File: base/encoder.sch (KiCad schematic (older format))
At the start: 4 parts

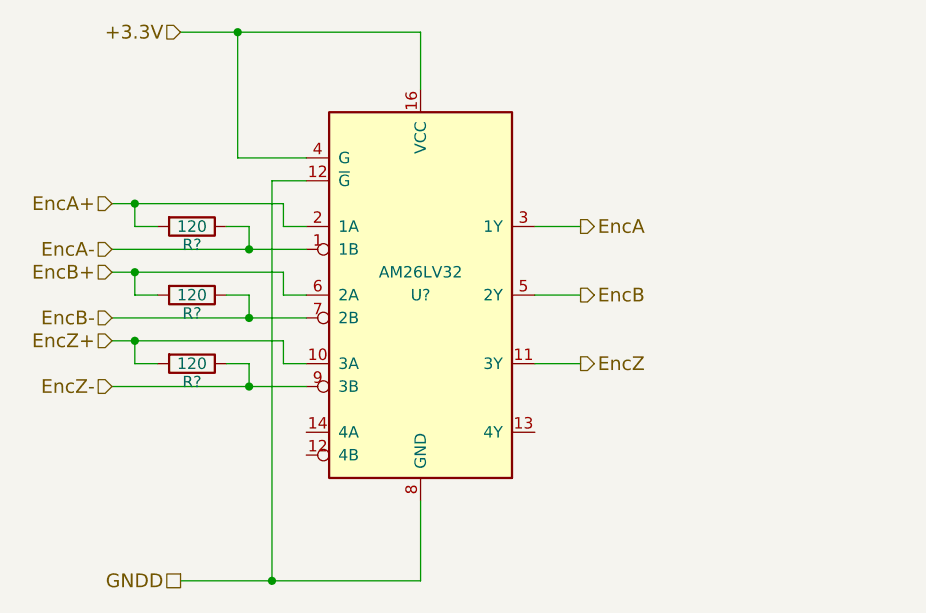
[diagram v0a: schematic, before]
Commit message: Update base board: 1. Add extra analog voltage input to core board.   -> update pinmux 2. Assign most footprints. 3. Generate netlist. 4. Add core_sf board. 5. Add kicad_symbols library submodule.
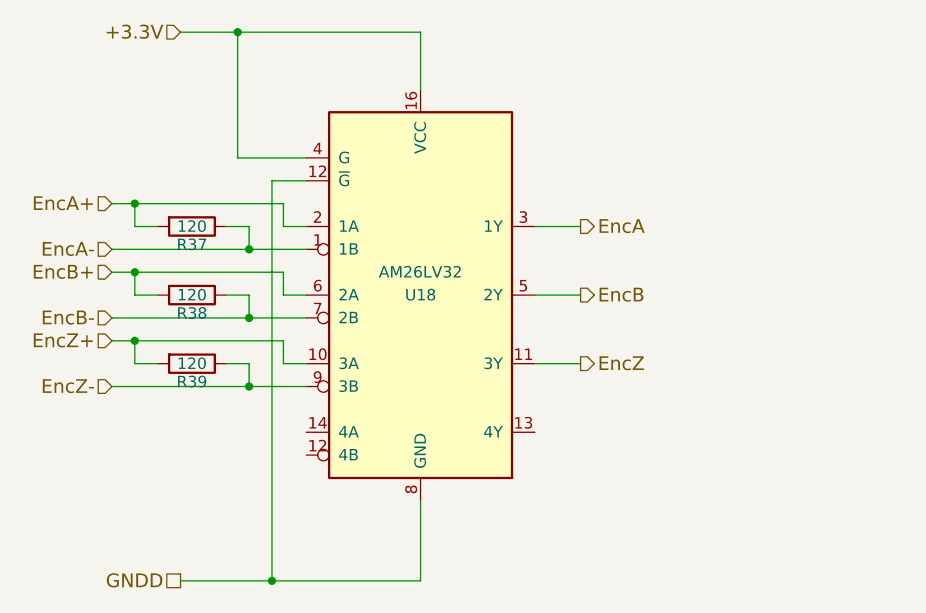
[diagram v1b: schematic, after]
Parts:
- R37, R38, R39: renamed from R?; footprint (none) -> Resistor_SMD:R_0603_1608Metric
- U18: renamed from U?; footprint Housings_SOIC:SOIC-16_3.9x9.9mm_Pitch1.27mm -> Package_SOIC:SOIC-16_3.9x9.9mm_P1.27mm
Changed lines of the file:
@@
 GNDD
 $Comp
-L AM26LV32 U?
+L AM26LV32 U18
 U 1 1 5A42515F
 P 4800 3250
-F 0 "U?" H 4800 3250 50  0000 C CNN
+F 0 "U18" H 4800 3250 50  0000 C CNN
 F 1 "AM26LV32" H 4800 3350 50  0000 C CNN
-F 2 "Housings_SOIC:SOIC-16_3.9x9.9mm_Pitch1.27mm" H 4900 2300 50  0001 C CNN
+F 2 "Package_SOIC:SOIC-16_3.9x9.9mm_P1.27mm" H 4900 2300 50  0001 C CNN
 F 3 "" H 4800 3250 50  0001 C CNN
 	1    4800 3250
@@
 Connection ~ 4150 4500
 $Comp
-L R R?
+L R R37
 U 1 1 5A425215
 P 3800 2950
-F 0 "R?" V 3880 2950 50  0000 C CNN
+F 0 "R37" V 3880 2950 50  0000 C CNN
 F 1 "120" V 3800 2950 50  0000 C CNN
-F 2 "" V 3730 2950 50  0001 C CNN
+F 2 "Resistor_SMD:R_0603_1608Metric" V 3730 2950 50  0001 C CNN
 F 3 "" H 3800 2950 50  0001 C CNN
 	1    3800 2950
@@
 	3450 3350 4300 3350
 $Comp
-L R R?
+L R R38
 U 1 1 5A425315
 P 3800 3250
-F 0 "R?" V 3880 3250 50  0000 C CNN
+F 0 "R38" V 3880 3250 50  0000 C CNN
 F 1 "120" V 3800 3250 50  0000 C CNN
-F 2 "" V 3730 3250 50  0001 C CNN
+F 2 "Resistor_SMD:R_0603_1608Metric" V 3730 3250 50  0001 C CNN
 F 3 "" H 3800 3250 50  0001 C CNN
 	1    3800 3250
@@
 	4300 3650 3450 3650
 $Comp
-L R R?
+L R R39
 U 1 1 5A425470
 P 3800 3550
-F 0 "R?" V 3880 3550 50  0000 C CNN
+F 0 "R39" V 3880 3550 50  0000 C CNN
 F 1 "120" V 3800 3550 50  0000 C CNN
-F 2 "" V 3730 3550 50  0001 C CNN
+F 2 "Resistor_SMD:R_0603_1608Metric" V 3730 3550 50  0001 C CNN
 F 3 "" H 3800 3550 50  0001 C CNN
 	1    3800 3550

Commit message: temp-sens-fan was created
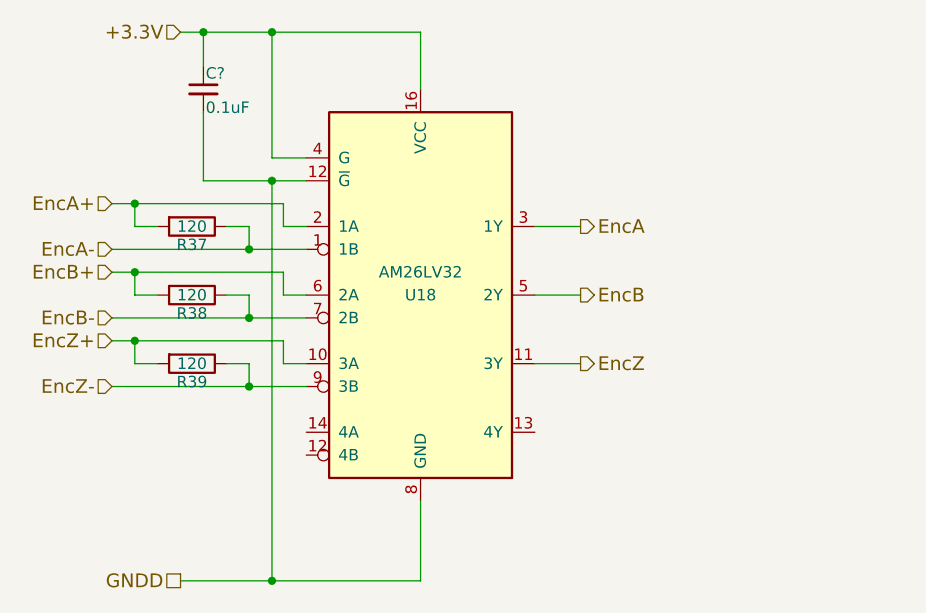
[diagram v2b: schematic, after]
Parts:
- added C?: 0.1uF, Capacitor_SMD:C_0603_1608Metric, symbol C_Small
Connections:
- net +3.3V: now also C?.1
- net GNDD: now also C?.2
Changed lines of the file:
@@
 LIBS:texas
 LIBS:opto
+LIBS:maxim
 LIBS:4hbd-base-cache
 EELAYER 25 0
@@
 	4800 2100 4800 2350
 Wire Wire Line
-	4300 2650 4000 2650
+	4300 2650 4150 2650
 Wire Wire Line
-	4000 2650 4000 2100
-Connection ~ 4000 2100
+	4150 2650 4150 2100
+Connection ~ 4150 2100
 Wire Wire Line
 	3750 4500 4800 4500
@@
 	4800 4500 4800 4150
 Wire Wire Line
-	4300 2750 4150 2750
+	3850 2750 4300 2750
 Wire Wire Line
 	4150 2750 4150 4500
@@
 Connection ~ 4050 3050
 Wire Wire Line
-	4300 3650 3450 3650
+	3450 3650 4300 3650
 $Comp
 L R R39
@@
 Wire Wire Line
 	5300 3550 5500 3550
+$Comp
+L C_Small C?
+U 1 1 5A47F1CB
+P 3850 2350
+F 0 "C?" H 3860 2420 50  0000 L CNN
+F 1 "0.1uF" H 3860 2270 50  0000 L CNN
+F 2 "Capacitor_SMD:C_0603_1608Metric" H 3850 2350 50  0001 C CNN
+F 3 "" H 3850 2350 50  0001 C CNN
+	1    3850 2350
+	1    0    0    -1
+$EndComp
+Wire Wire Line
+	3850 2750 3850 2450
+Connection ~ 4150 2750
+Wire Wire Line
+	3850 2250 3850 2100
+Connection ~ 3850 2100
 $EndSCHEMATC

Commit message: annotate sch
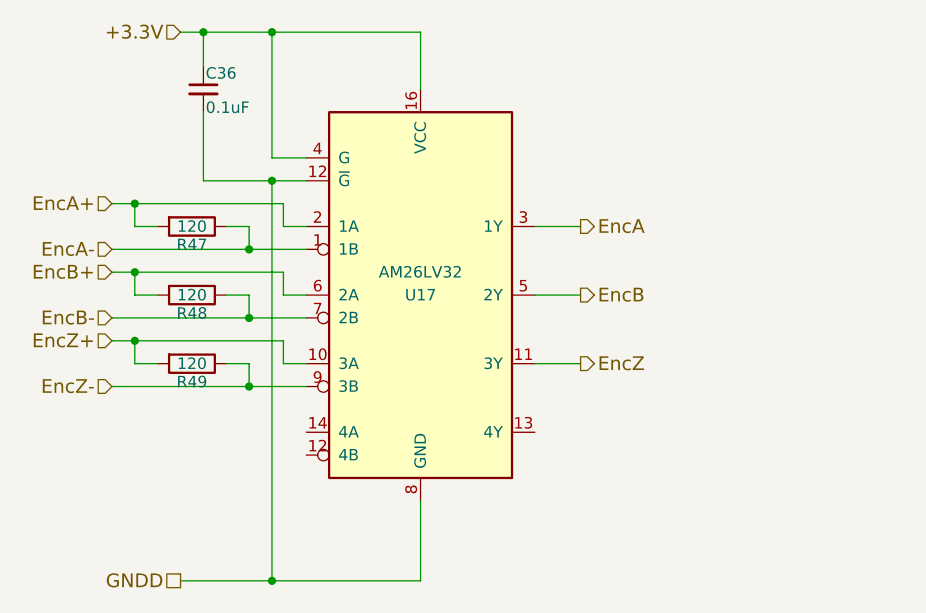
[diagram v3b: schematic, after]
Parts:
- gave numbers to parts that had none: 1
- renumbered R37 to R47, R38 to R48, R39 to R49, U18 to U17
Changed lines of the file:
@@
 GNDD
 $Comp
-L AM26LV32 U18
+L AM26LV32 U17
 U 1 1 5A42515F
 P 4800 3250
-F 0 "U18" H 4800 3250 50  0000 C CNN
+F 0 "U17" H 4800 3250 50  0000 C CNN
 F 1 "AM26LV32" H 4800 3350 50  0000 C CNN
 F 2 "Package_SOIC:SOIC-16_3.9x9.9mm_P1.27mm" H 4900 2300 50  0001 C CNN
@@
 Connection ~ 4150 4500
 $Comp
-L R R37
+L R R47
 U 1 1 5A425215
 P 3800 2950
-F 0 "R37" V 3880 2950 50  0000 C CNN
+F 0 "R47" V 3880 2950 50  0000 C CNN
 F 1 "120" V 3800 2950 50  0000 C CNN
 F 2 "Resistor_SMD:R_0603_1608Metric" V 3730 2950 50  0001 C CNN
@@
 	3450 3350 4300 3350
 $Comp
-L R R38
+L R R48
 U 1 1 5A425315
 P 3800 3250
-F 0 "R38" V 3880 3250 50  0000 C CNN
+F 0 "R48" V 3880 3250 50  0000 C CNN
 F 1 "120" V 3800 3250 50  0000 C CNN
 F 2 "Resistor_SMD:R_0603_1608Metric" V 3730 3250 50  0001 C CNN
@@
 	3450 3650 4300 3650
 $Comp
-L R R39
+L R R49
 U 1 1 5A425470
 P 3800 3550
-F 0 "R39" V 3880 3550 50  0000 C CNN
+F 0 "R49" V 3880 3550 50  0000 C CNN
 F 1 "120" V 3800 3550 50  0000 C CNN
 F 2 "Resistor_SMD:R_0603_1608Metric" V 3730 3550 50  0001 C CNN
@@
 	5300 3550 5500 3550
 $Comp
-L C_Small C?
+L C_Small C36
 U 1 1 5A47F1CB
 P 3850 2350
-F 0 "C?" H 3860 2420 50  0000 L CNN
+F 0 "C36" H 3860 2420 50  0000 L CNN
 F 1 "0.1uF" H 3860 2270 50  0000 L CNN
 F 2 "Capacitor_SMD:C_0603_1608Metric" H 3850 2350 50  0001 C CNN

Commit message: assign footprints
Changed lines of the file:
@@
 U 1 1 5A42515F
 P 4800 3250
-F 0 "U17" H 4800 3250 50  0000 C CNN
+F 0 "U17" H 5100 4150 50  0000 C CNN
 F 1 "AM26LV32" H 4800 3350 50  0000 C CNN
 F 2 "Package_SOIC:SOIC-16_3.9x9.9mm_P1.27mm" H 4900 2300 50  0001 C CNN

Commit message: upd
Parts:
- renumbered C36 to C34
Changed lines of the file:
@@
 	5300 3550 5500 3550
 $Comp
-L C_Small C36
+L C_Small C34
 U 1 1 5A47F1CB
 P 3850 2350
-F 0 "C36" H 3860 2420 50  0000 L CNN
+F 0 "C34" H 3860 2420 50  0000 L CNN
 F 1 "0.1uF" H 3860 2270 50  0000 L CNN
 F 2 "Capacitor_SMD:C_0603_1608Metric" H 3850 2350 50  0001 C CNN

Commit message: upd
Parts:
- added R19, R20, R21: 10k, Resistor_SMD:R_0603_1608Metric, symbol R
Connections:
- net +3.3V: now also R19.2, R20.2, R21.2
- net EncA: now also R19.1
- net EncB: now also R20.1
- net EncZ: now also R21.1
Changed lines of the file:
@@
 Comment4 ""
 $EndDescr
-Text HLabel 5500 2950 2    60   Output ~ 0
+Text HLabel 6600 2950 2    60   Output ~ 0
 EncA
-Text HLabel 5500 3250 2    60   Output ~ 0
+Text HLabel 6600 3250 2    60   Output ~ 0
 EncB
-Text HLabel 5500 3550 2    60   Output ~ 0
+Text HLabel 6600 3550 2    60   Output ~ 0
 EncZ
 Text HLabel 3450 2850 0    60   Input ~ 0
@@
 	1    0    0    -1
 $EndComp
-Wire Wire Line
-	3750 2100 4800 2100
-Wire Wire Line
-	4800 2100 4800 2350
-Wire Wire Line
-	4300 2650 4150 2650
-Wire Wire Line
-	4150 2650 4150 2100
-Connection ~ 4150 2100
-Wire Wire Line
-	3750 4500 4800 4500
-Wire Wire Line
-	4800 4500 4800 4150
-Wire Wire Line
-	3850 2750 4300 2750
-Wire Wire Line
-	4150 2750 4150 4500
-Connection ~ 4150 4500
 $Comp
 L R R47
@@
 	0    1    1    0
 $EndComp
-Wire Wire Line
-	3450 2850 4200 2850
-Wire Wire Line
-	4200 2850 4200 2950
-Wire Wire Line
-	4200 2950 4300 2950
-Wire Wire Line
-	3450 3050 4300 3050
-Wire Wire Line
-	3550 2850 3550 2950
-Connection ~ 3550 2850
-Wire Wire Line
-	3450 3150 4200 3150
-Wire Wire Line
-	4200 3150 4200 3250
-Wire Wire Line
-	4200 3250 4300 3250
-Wire Wire Line
-	3450 3350 4300 3350
 $Comp
 L R R48
@@
 	0    1    1    0
 $EndComp
-Wire Wire Line
-	3650 3250 3550 3250
-Wire Wire Line
-	3550 3250 3550 3150
-Connection ~ 3550 3150
-Wire Wire Line
-	3950 3250 4050 3250
-Wire Wire Line
-	4050 3250 4050 3350
-Connection ~ 4050 3350
-Wire Wire Line
-	3950 2950 4050 2950
-Wire Wire Line
-	3550 2950 3650 2950
-Wire Wire Line
-	4050 2950 4050 3050
-Connection ~ 4050 3050
-Wire Wire Line
-	3450 3650 4300 3650
 $Comp
 L R R49
@@
 	0    1    1    0
 $EndComp
-Wire Wire Line
-	3450 3450 4200 3450
-Wire Wire Line
-	4200 3450 4200 3550
-Wire Wire Line
-	4200 3550 4300 3550
-Wire Wire Line
-	3950 3550 4050 3550
-Wire Wire Line
-	4050 3550 4050 3650
-Connection ~ 4050 3650
-Wire Wire Line
-	3650 3550 3550 3550
-Wire Wire Line
-	3550 3550 3550 3450
-Connection ~ 3550 3450
-Wire Wire Line
-	5300 2950 5500 2950
-Wire Wire Line
-	5300 3250 5500 3250
-Wire Wire Line
-	5300 3550 5500 3550
 $Comp
 L C_Small C34
@@
 	1    0    0    -1
 $EndComp
+$Comp
+L R R19
+U 1 1 5AA4913C
+P 5950 2700
+F 0 "R19" V 6030 2700 50  0000 C CNN
+F 1 "10k" V 5950 2700 50  0000 C CNN
+F 2 "Resistor_SMD:R_0603_1608Metric" V 5880 2700 50  0001 C CNN
+F 3 "" H 5950 2700 50  0001 C CNN
+	1    5950 2700
+	-1   0    0    1
+$EndComp
+$Comp
+L R R20
+U 1 1 5AA49248
+P 6150 2700
+F 0 "R20" V 6230 2700 50  0000 C CNN
+F 1 "10k" V 6150 2700 50  0000 C CNN
+F 2 "Resistor_SMD:R_0603_1608Metric" V 6080 2700 50  0001 C CNN
+F 3 "" H 6150 2700 50  0001 C CNN
+	1    6150 2700
+	-1   0    0    1
+$EndComp
+$Comp
+L R R21
+U 1 1 5AA49277
+P 6350 2700
+F 0 "R21" V 6430 2700 50  0000 C CNN
+F 1 "10k" V 6350 2700 50  0000 C CNN
+F 2 "Resistor_SMD:R_0603_1608Metric" V 6280 2700 50  0001 C CNN
+F 3 "" H 6350 2700 50  0001 C CNN
+	1    6350 2700
+	-1   0    0    1
+$EndComp
+Wire Wire Line
+	3750 2100 6350 2100
+Wire Wire Line
+	4800 2100 4800 2350
+Wire Wire Line
+	4300 2650 4150 2650
+Wire Wire Line
+	4150 2650 4150 2100
+Connection ~ 4150 2100
+Wire Wire Line
+	3750 4500 4800 4500
+Wire Wire Line
+	4800 4500 4800 4150
+Wire Wire Line
+	3850 2750 4300 2750
+Wire Wire Line
+	4150 2750 4150 4500
+Connection ~ 4150 4500
+Wire Wire Line
+	3450 2850 4200 2850
+Wire Wire Line
+	4200 2850 4200 2950
+Wire Wire Line
+	4200 2950 4300 2950
+Wire Wire Line
+	3450 3050 4300 3050
+Wire Wire Line
+	3550 2850 3550 2950
+Connection ~ 3550 2850
+Wire Wire Line
+	3450 3150 4200 3150
+Wire Wire Line
+	4200 3150 4200 3250
+Wire Wire Line
+	4200 3250 4300 3250
+Wire Wire Line
+	3450 3350 4300 3350
+Wire Wire Line
+	3650 3250 3550 3250
+Wire Wire Line
+	3550 3250 3550 3150
+Connection ~ 3550 3150
+Wire Wire Line
+	3950 3250 4050 3250
+Wire Wire Line
+	4050 3250 4050 3350
+Connection ~ 4050 3350
+Wire Wire Line
+	3950 2950 4050 2950
+Wire Wire Line
+	3550 2950 3650 2950
+Wire Wire Line
+	4050 2950 4050 3050
+Connection ~ 4050 3050
+Wire Wire Line
+	3450 3650 4300 3650
+Wire Wire Line
+	3450 3450 4200 3450
+Wire Wire Line
+	4200 3450 4200 3550
+Wire Wire Line
+	4200 3550 4300 3550
+Wire Wire Line
+	3950 3550 4050 3550
+Wire Wire Line
+	4050 3550 4050 3650
+Connection ~ 4050 3650
+Wire Wire Line
+	3650 3550 3550 3550
+Wire Wire Line
+	3550 3550 3550 3450
+Connection ~ 3550 3450
+Wire Wire Line
+	5300 2950 6600 2950
+Wire Wire Line
+	5300 3250 6600 3250
+Wire Wire Line
+	5300 3550 6600 3550
 Wire Wire Line
 	3850 2750 3850 2450
@@
 	3850 2250 3850 2100
 Connection ~ 3850 2100
+Wire Wire Line
+	5950 2850 5950 2950
+Connection ~ 5950 2950
+Wire Wire Line
+	6150 2850 6150 3250
+Connection ~ 6150 3250
+Wire Wire Line
+	6350 2850 6350 3550
+Connection ~ 6350 3550
+Wire Wire Line
+	5950 2100 5950 2550
+Connection ~ 4800 2100
+Wire Wire Line
+	6150 2100 6150 2550
+Connection ~ 5950 2100
+Wire Wire Line
+	6350 2100 6350 2550
+Connection ~ 6150 2100
 $EndSCHEMATC
